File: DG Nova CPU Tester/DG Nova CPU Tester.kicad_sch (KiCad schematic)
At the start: 121 parts, among them J1 Slot_02x50_Odd_Even, J10 Programmed I/O, J11 CPU Option Inputs, J12 Data Channel, J13 Program Interrupt, J14 System Control, J17 CPU Option Outputs, J18 MEM Control Outputs, J19 Logic 8 CH, J20 Logic 8 CH, J21 Arduino Anolog Pins, J22 Arduino Digital Pins, J23 Arduino Digital Pins, J4 ATX Power Port, J6 MBO, J7 MEM, J8 Data Channel, J9 Front Panel Controls, SW1 Arduino Mega Reset, SW1 Pico Reset, SW2 Power Swtich, U1 74HC14, U2 Pico

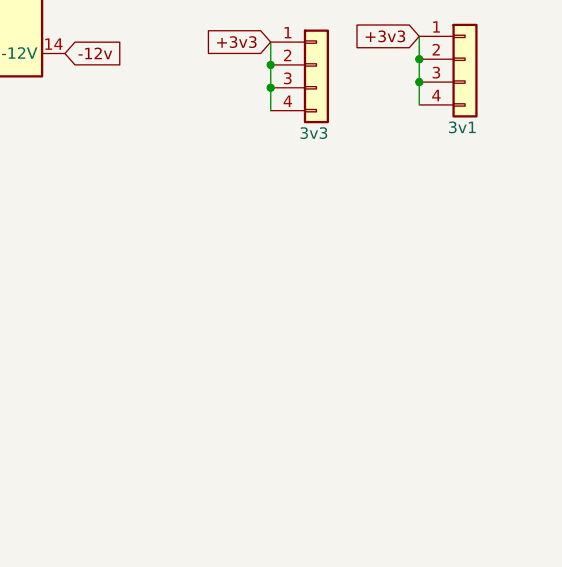
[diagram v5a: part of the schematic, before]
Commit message: 3v3 to 5v work
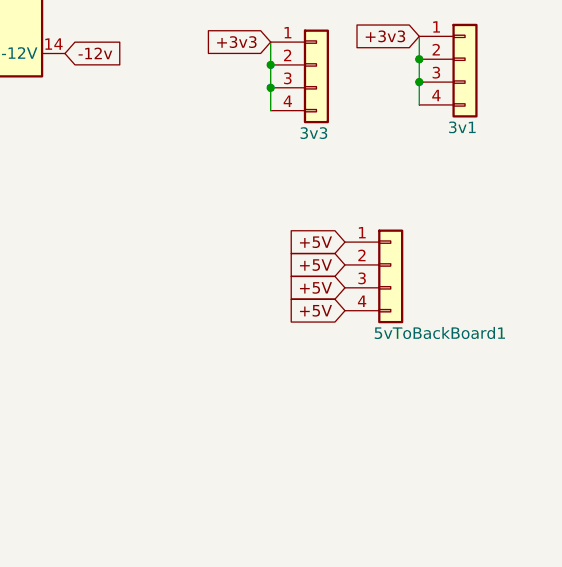
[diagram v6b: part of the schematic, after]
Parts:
- added 5vToBackBoard1: 3v3, Connector_PinHeader_2.54mm:PinHeader_1x04_P2.54mm_Vertical, symbol Connector_Generic:Conn_01x04
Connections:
- net +5V: now also 5vToBackBoard1.1 (Pin_1), 5vToBackBoard1.2 (Pin_2), 5vToBackBoard1.3 (Pin_3), 5vToBackBoard1.4 (Pin_4)
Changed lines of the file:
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@@
     )
   )
+  (global_label "+5V" (shape input) (at 430.53 115.57 180) (fields_autoplaced)
+    (effects (font (size 1.27 1.27)) (justify right))
+    (property "Intersheetrefs" "${INTERSHEET_REFS}" (at 424.3285 115.57 0)
+      (effects (font (size 1.27 1.27)) (justify right) hide)
+    )
+  )
   (global_label "~{MBO15}" (shape input) (at 64.135 2.54 180) (fields_autoplaced)
     (effects (font (size 1.27 1.27)) (justify right))
@@
     )
   )
+  (global_label "+5V" (shape input) (at 430.53 110.49 180) (fields_autoplaced)
+    (effects (font (size 1.27 1.27)) (justify right))
+    (property "Intersheetrefs" "${INTERSHEET_REFS}" (at 424.3285 110.49 0)
+      (effects (font (size 1.27 1.27)) (justify right) hide)
+    )
+  )
   (global_label "~{FETCH}" (shape input) (at 213.36 266.065 0) (fields_autoplaced)
     (effects (font (size 1.27 1.27)) (justify left))
@@
     )
   )
+  (global_label "+5V" (shape input) (at 430.53 113.03 180) (fields_autoplaced)
+    (effects (font (size 1.27 1.27)) (justify right))
+    (property "Intersheetrefs" "${INTERSHEET_REFS}" (at 424.3285 113.03 0)
+      (effects (font (size 1.27 1.27)) (justify right) hide)
+    )
+  )
   (global_label "~{SELD}" (shape input) (at 213.995 3.81 0) (fields_autoplaced)
     (effects (font (size 1.27 1.27)) (justify left))
@@
     )
   )
+  (global_label "+5V" (shape input) (at 430.53 107.95 180) (fields_autoplaced)
+    (effects (font (size 1.27 1.27)) (justify right))
+    (property "Intersheetrefs" "${INTERSHEET_REFS}" (at 424.3285 107.95 0)
+      (effects (font (size 1.27 1.27)) (justify right) hide)
+    )
+  )
   (global_label "~{DATA1}" (shape input) (at 291.465 311.15 90) (fields_autoplaced)
     (effects (font (size 1.27 1.27)) (justify left))
@@
         )
       )
+    )
+  )
+  (symbol (lib_id "Connector_Generic:Conn_01x04") (at 435.61 110.49 0) (unit 1)
+    (in_bom yes) (on_board yes) (dnp no)
+    (property "Reference" "5vToBackBoard1" (at 433.705 118.11 0)
+      (effects (font (size 1.27 1.27)) (justify left))
+    )
+    (property "Value" "3v3" (at 438.15 113.665 0)
+      (effects (font (size 1.27 1.27)) (justify left) hide)
+    )
+    (property "Footprint" "Connector_PinHeader_2.54mm:PinHeader_1x04_P2.54mm_Vertical" (at 435.61 110.49 0)
+      (effects (font (size 1.27 1.27)) hide)
+    )
+    (property "Datasheet" "~" (at 435.61 110.49 0)
+      (effects (font (size 1.27 1.27)) hide)
+    )
+    (pin "1")
+    (pin "2")
+    (pin "3")
+    (pin "4")
+    (instances
+      (project "DG Nova CPU Tester"
+        (path "/c1f710ce-b3f9-4828-9325-9c2326e8d74c"
+          (reference "5vToBackBoard1") (unit 1)
+        )
+      )

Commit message: Updates
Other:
- note removed: "Reverse Footprint "backside""
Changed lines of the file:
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@@
-    (effects (font (size 1.27 1.27)) (justify left bottom))
-  )
-  (text "Reverse Footprint \"backside\"" (at 278.765 111.76 0)
     (effects (font (size 1.27 1.27)) (justify left bottom))
   )

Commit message: QuantX schematic update
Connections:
- net GND: now also J19.9 (Pin_9)
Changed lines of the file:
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@@
+    )
+  )
+  (global_label "GND" (shape input) (at 284.48 105.41 180) (fields_autoplaced)
+    (effects (font (size 1.27 1.27)) (justify right))
+    (property "Intersheetrefs" "${INTERSHEET_REFS}" (at 278.2785 105.41 0)
+      (effects (font (size 1.27 1.27)) (justify right) hide)
     )
   )
